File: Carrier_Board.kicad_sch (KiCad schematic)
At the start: 6 parts

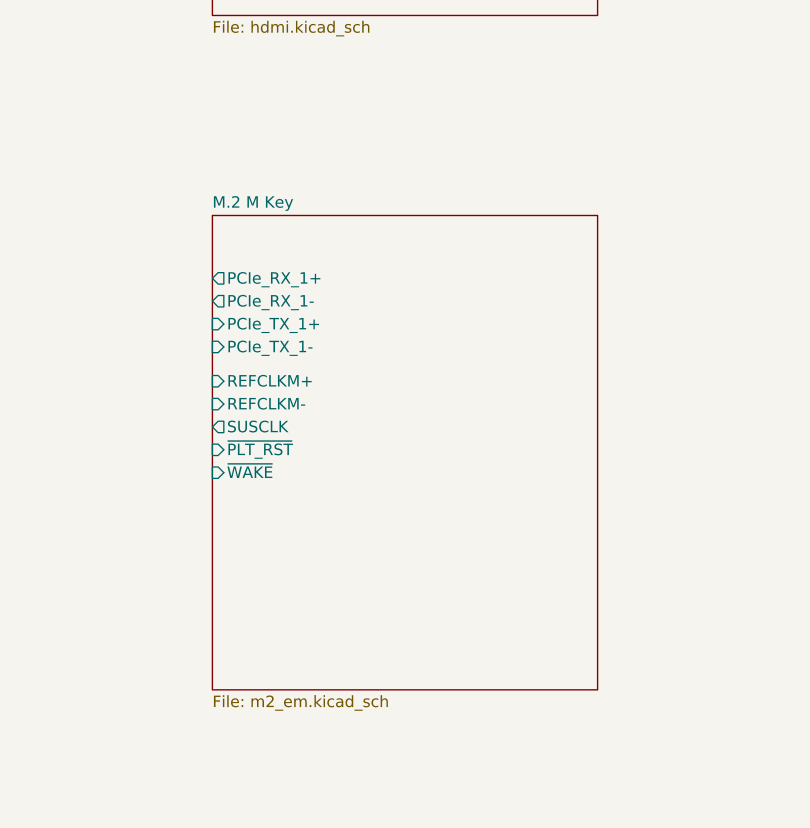
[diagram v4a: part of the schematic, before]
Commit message: Finished the shematic capture of the M.2 sheet but still have to assign the footprints
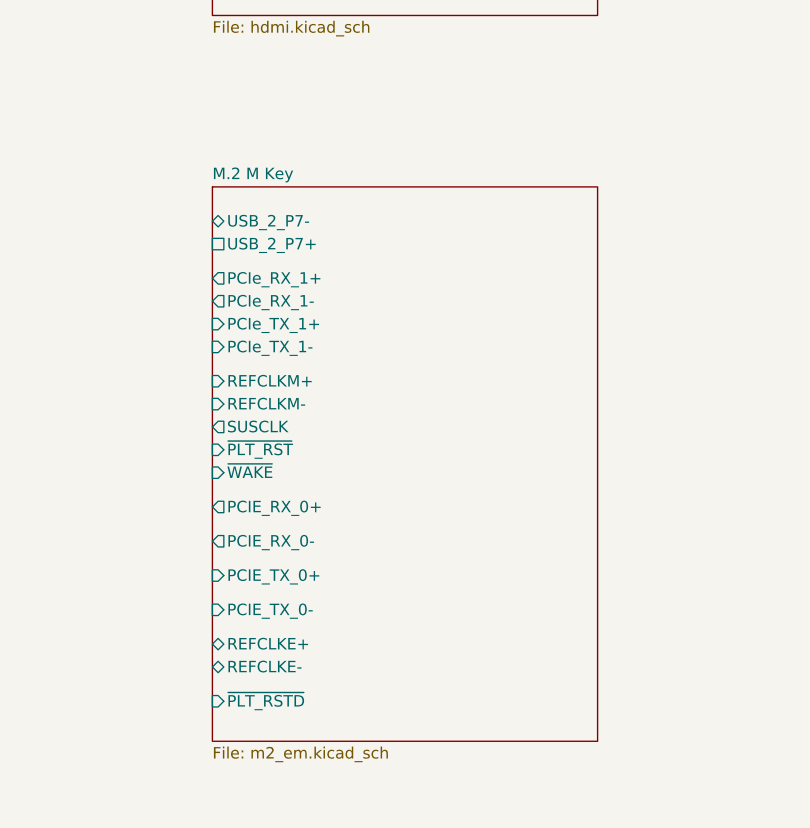
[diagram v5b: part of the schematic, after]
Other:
- sheet M.2 M Key ports: added PCIE_RX_0+, PCIE_RX_0-, PCIE_TX_0+, PCIE_TX_0-, REFCLKE+, REFCLKE-, USB_2_P7+, USB_2_P7-, ~{PLT_RSTD}; removed none
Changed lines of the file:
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@@
 	)
 	(sheet
-		(at 329.946 321.945)
-		(size 42.799 52.705)
+		(at 329.946 318.77)
+		(size 42.799 61.595)
 		(exclude_from_sim no)
 		(in_bom yes)
@@
 		)
 		(property "Sheetname" "M.2 M Key"
-			(at 329.946 321.2334 0)
+			(at 329.946 318.0584 0)
 			(show_name no)
 			(do_not_autoplace no)
@@
 		)
 		(property "Sheetfile" "m2_em.kicad_sch"
-			(at 329.946 375.2346 0)
+			(at 329.946 380.9496 0)
 			(show_name no)
 			(do_not_autoplace no)
@@
 			(effects
 				(font
+					(size 1.27 1.27)
+				)
+				(justify left)
+			)
+		)
+		(pin "PCIE_RX_0+" output
+			(at 329.946 354.33 180)
+			(effects
+				(font
+					(size 1.27 1.27)
+				)
+				(justify left)
+			)
+		)
+		(pin "PCIE_RX_0-" output
+			(at 329.946 358.14 180)
+			(effects
+				(font
+					(size 1.27 1.27)
+				)
+				(justify left)
+			)
+		)
+		(pin "PCIE_TX_0+" input
+			(at 329.946 361.95 180)
+			(effects
+				(font
+					(size 1.27 1.27)
+				)
+				(justify left)
+			)
+		)
+		(pin "PCIE_TX_0-" input
+			(at 329.946 365.76 180)
+			(effects
+				(font
+					(size 1.27 1.27)
+				)
+				(justify left)
+			)
+		)
+		(pin "REFCLKE+" bidirectional
+			(at 329.946 369.57 180)
+			(effects
+				(font
+					(size 1.27 1.27)
+				)
+				(justify left)
+			)
+		)
+		(pin "REFCLKE-" bidirectional
+			(at 329.946 372.11 180)
+			(effects
+				(font
+					(size 1.27 1.27)
+				)
+				(justify left)
+			)
+		)
+		(pin "USB_2_P7+" passive
+			(at 329.946 325.12 180)
+			(effects
+				(font
+					(size 1.27 1.27)
+				)
+				(justify left)
+			)
+		)
+		(pin "USB_2_P7-" bidirectional
+			(at 329.946 322.58 180)
+			(effects
+				(font
+					(size 1.27 1.27)
+				)
+				(justify left)
+			)
+		)
+		(pin "~{PLT_RSTD}" input
+			(at 329.946 375.92 180)
+			(effects
+				(font

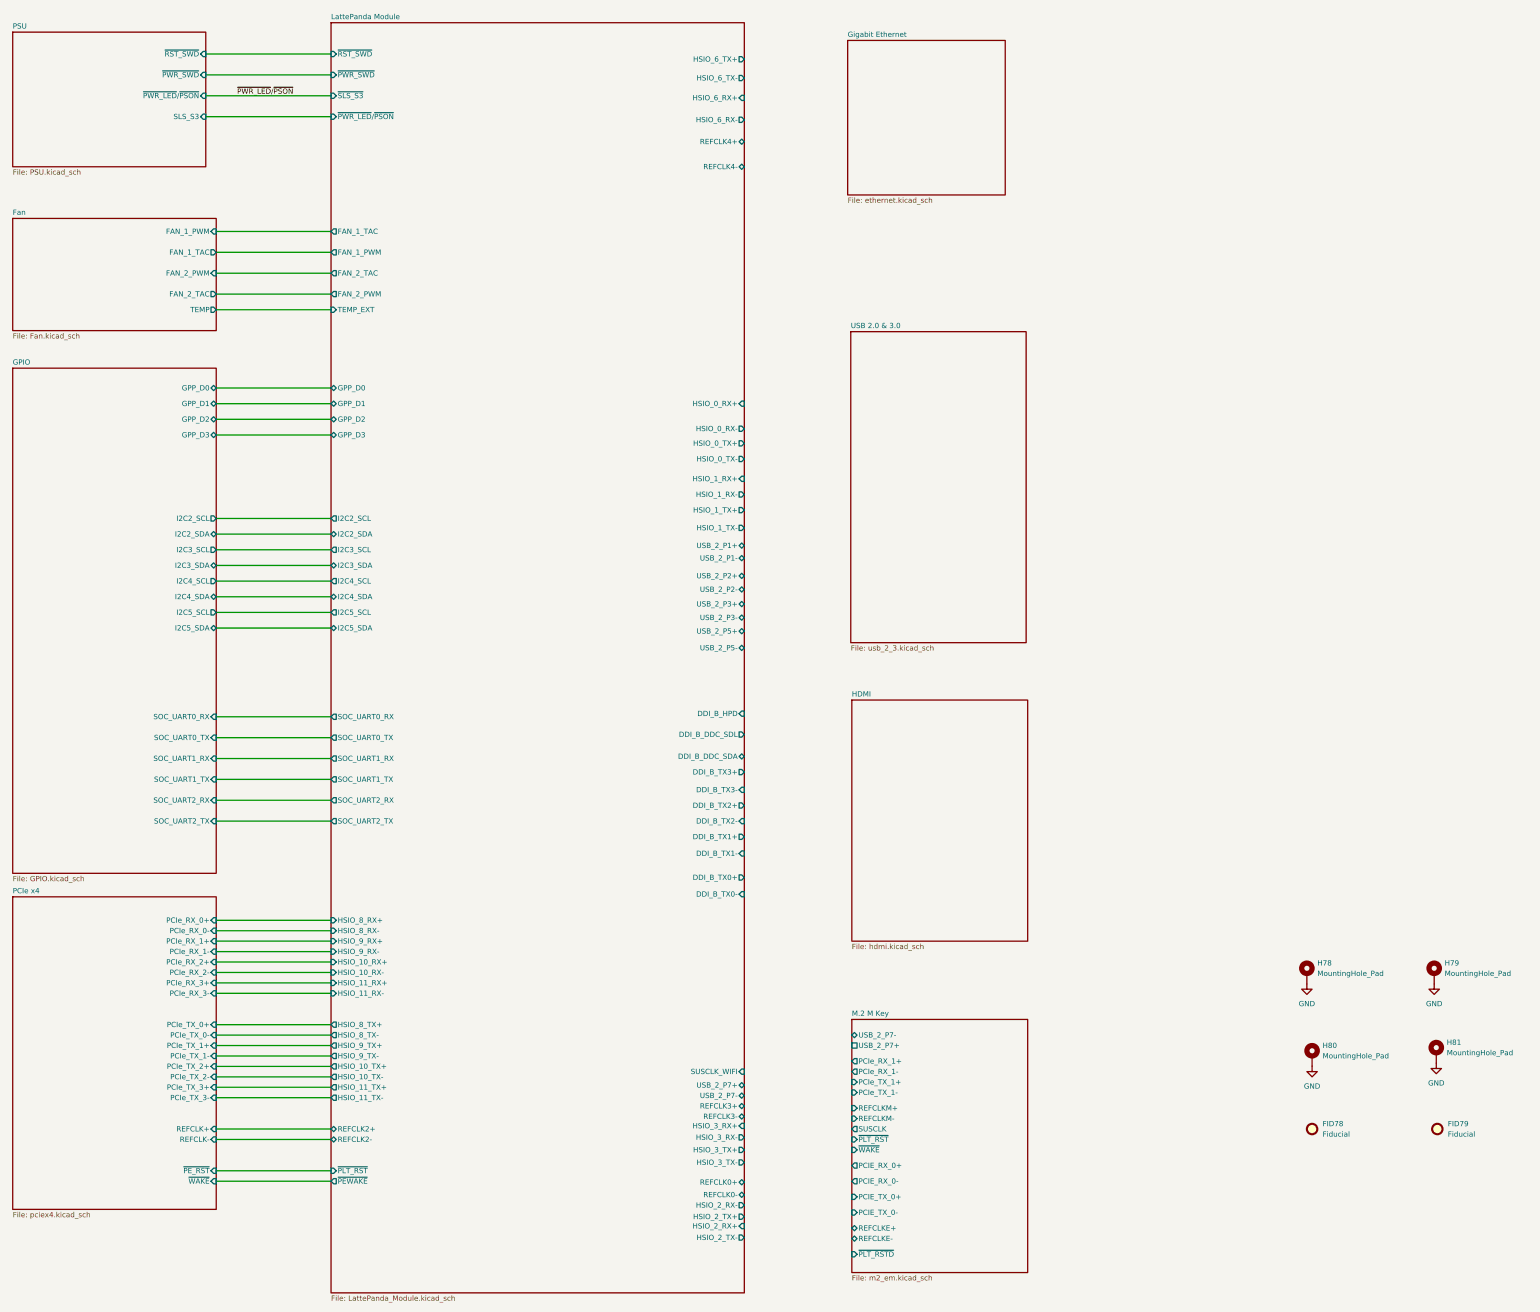
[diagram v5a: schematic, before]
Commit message: Connected the hierarchical labels in the root sheet to the gigabit ethernet
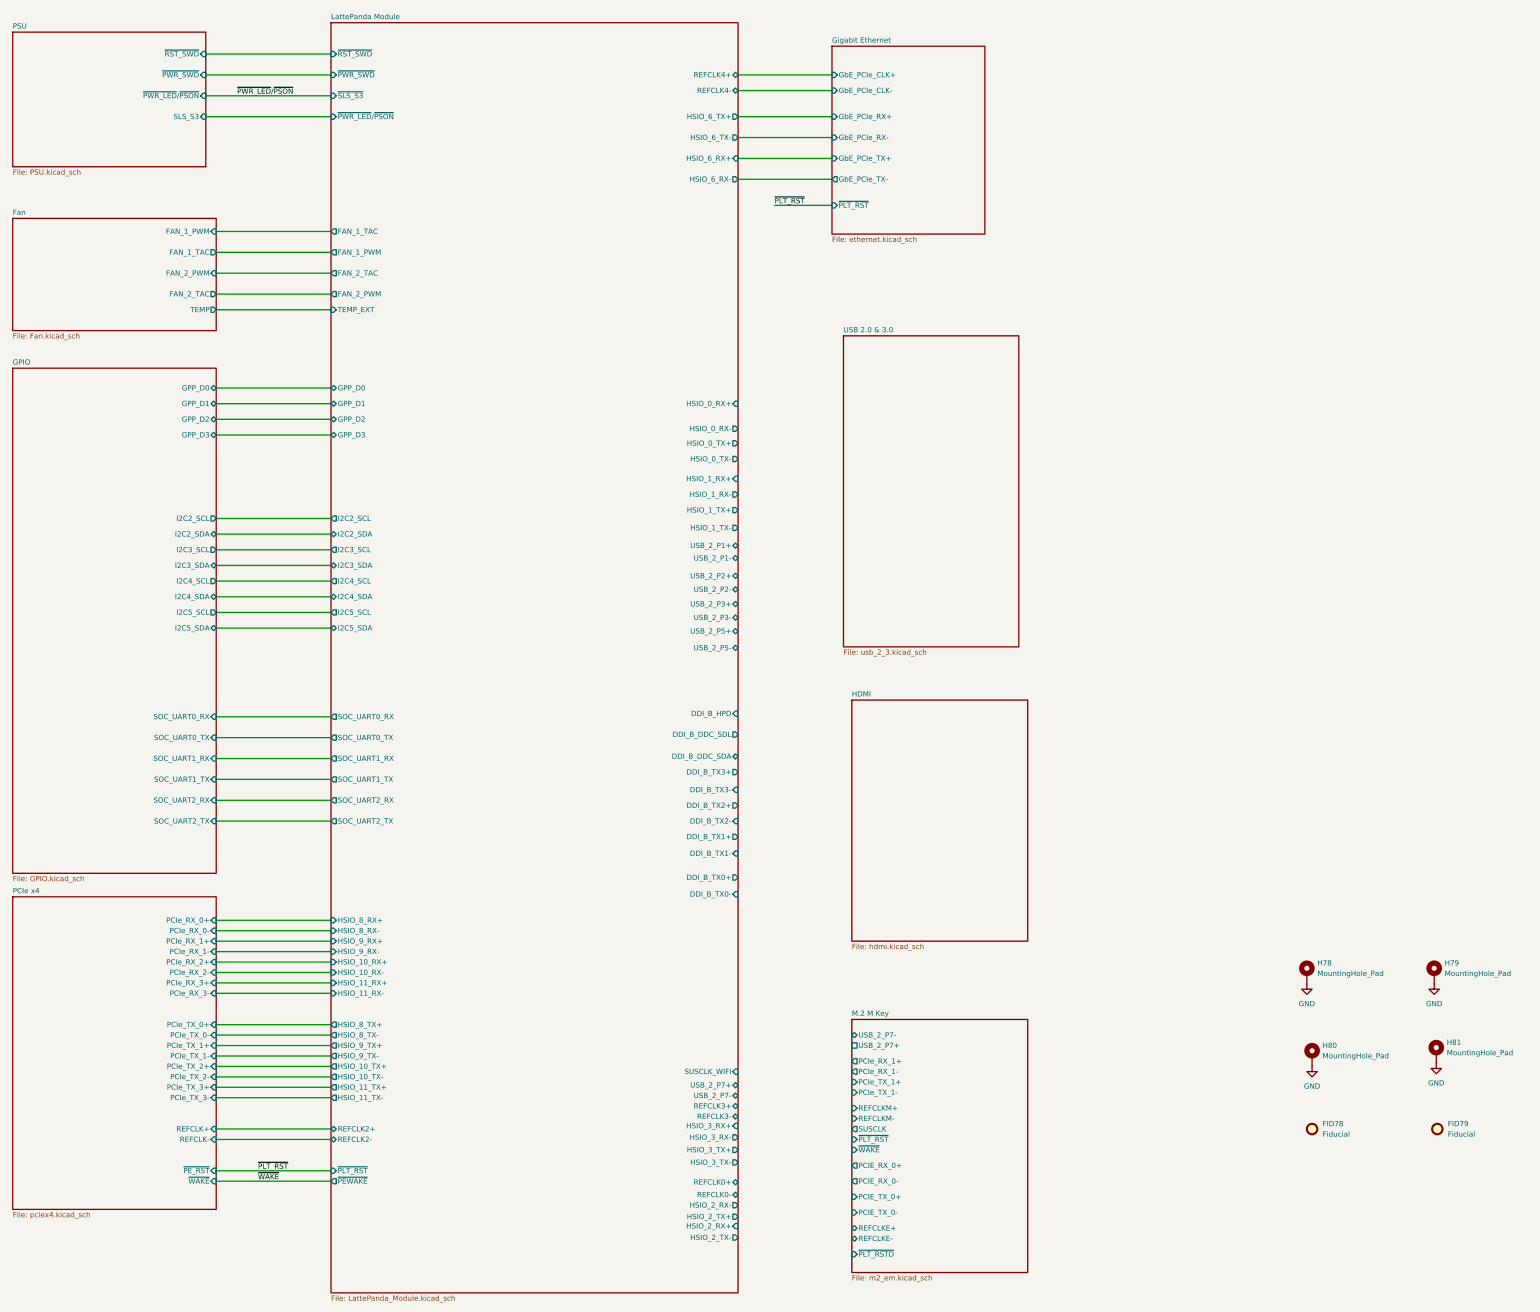
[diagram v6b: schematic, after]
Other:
- sheet Gigabit Ethernet ports: added GbE_PCIe_CLK+, GbE_PCIe_CLK-, GbE_PCIe_RX+, GbE_PCIe_RX-, GbE_PCIe_TX+, GbE_PCIe_TX-, ~{PLT_RST}; removed none

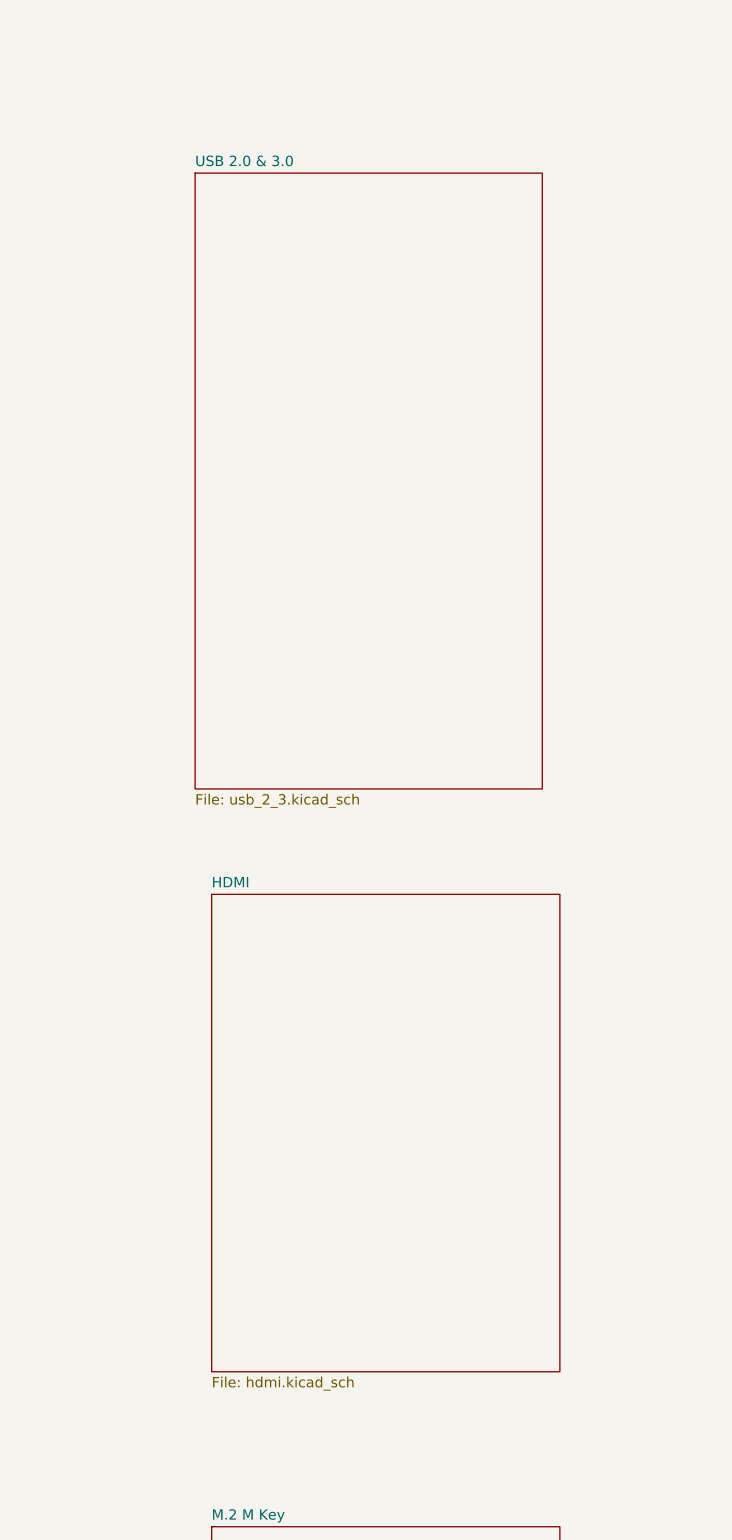
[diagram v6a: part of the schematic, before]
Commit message: Fixed some ERC errors int the gigabit sub schema
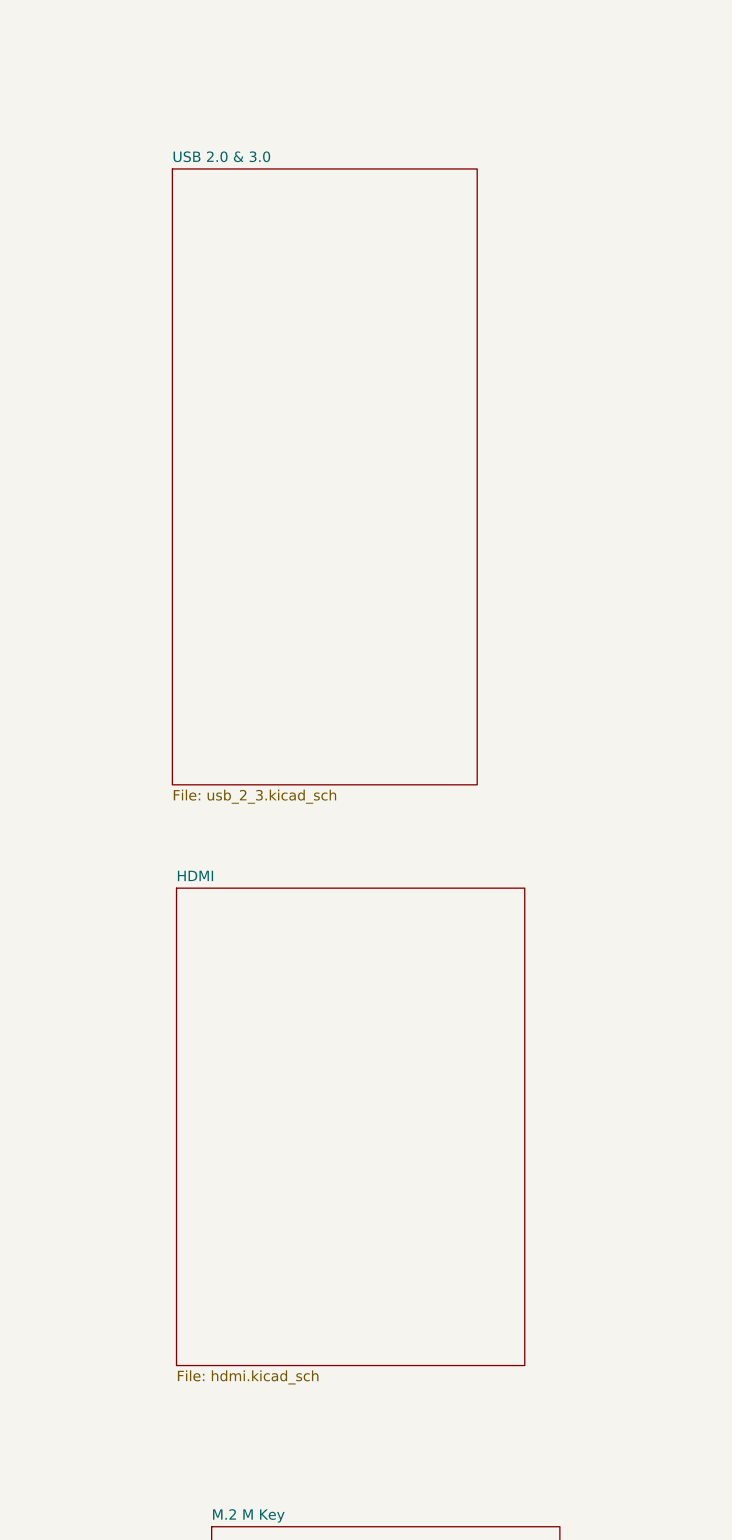
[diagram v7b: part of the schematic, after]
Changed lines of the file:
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@@
 	)
 	(sheet
-		(at 329.946 241.046)
+		(at 325.628 240.284)
 		(size 42.799 58.674)
 		(exclude_from_sim no)
@@
 		)
 		(property "Sheetname" "HDMI"
-			(at 329.946 240.3344 0)
+			(at 325.628 239.5724 0)
 			(show_name no)
 			(do_not_autoplace no)
@@
 		)
 		(property "Sheetfile" "hdmi.kicad_sch"
-			(at 329.946 300.3046 0)
+			(at 325.628 299.5426 0)
 			(show_name no)
 			(do_not_autoplace no)
@@
 	)
 	(sheet
-		(at 327.914 152.4)
-		(size 42.672 75.692)
+		(at 325.12 151.892)
+		(size 37.465 75.692)
 		(exclude_from_sim no)
 		(in_bom yes)
@@
 		)
 		(property "Sheetname" "USB 2.0 & 3.0"
-			(at 327.914 151.6884 0)
+			(at 325.12 151.1804 0)
 			(show_name no)
 			(do_not_autoplace no)
@@
 		)
 		(property "Sheetfile" "usb_2_3.kicad_sch"
-			(at 327.914 228.6766 0)
+			(at 325.12 228.1686 0)
 			(show_name no)
 			(do_not_autoplace no)
